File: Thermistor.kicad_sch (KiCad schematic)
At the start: 15 parts, among them U10 TLV6001DCK, U11 TLV6001DCK, U12 TLV6001DCK

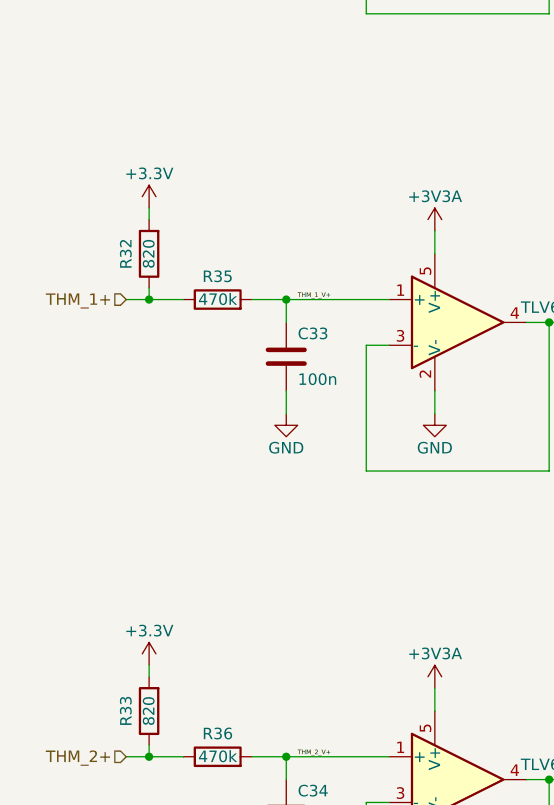
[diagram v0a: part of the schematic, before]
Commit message: Changed +3V3 to +3v3A for thermistor supplies
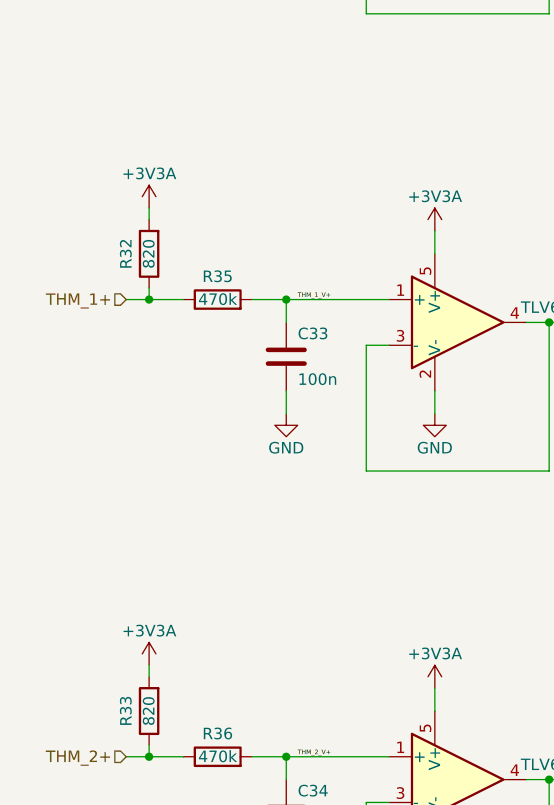
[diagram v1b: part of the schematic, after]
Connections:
- net +3.3V is gone; now on net +3V3A: R32.2, R33.2
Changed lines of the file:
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@@
-	)
-	(symbol
-		(lib_id "power:+3.3V")
-		(at 78.74 137.16 0)
-		(unit 1)
-		(exclude_from_sim no)
-		(in_bom yes)
-		(on_board yes)
-		(dnp no)
-		(property "Reference" "#PWR087"
-			(at 78.74 140.97 0)
-			(effects
-				(font
-					(size 1.27 1.27)
-				)
-				(hide yes)
-			)
-		)
-		(property "Value" "+3.3V"
-			(at 78.74 133.35 0)
-			(effects
-				(font
-					(size 1.27 1.27)
-				)
-			)
-		)
-		(property "Footprint" ""
-			(at 78.74 137.16 0)
-			(effects
-				(font
-					(size 1.27 1.27)
-				)
-				(hide yes)
-			)
-		)
-		(property "Datasheet" ""
-			(at 78.74 137.16 0)
-			(effects
-				(font
-					(size 1.27 1.27)
-				)
-				(hide yes)
-			)
-		)
-		(property "Description" "Power symbol creates a global label with name \"+3.3V\""
-			(at 78.74 137.16 0)
-			(effects
-				(font
-					(size 1.27 1.27)
-				)
-				(hide yes)
-			)
-		)
-		(pin "1"
-		)
-		(instances
-			(project "Motor_Control_Brain_Board"
-				(path "/7261d109-8405-40e9-921c-d95f374a7164/b4d68d60-4109-4352-9fbb-6372306ada14"
-					(reference "#PWR087")
-					(unit 1)
-				)
-			)
-		)
 	)
 	(symbol
@@
 	)
 	(symbol
+		(lib_id "power:+3.3VA")
+		(at 78.74 86.36 0)
+		(unit 1)
+		(exclude_from_sim no)
+		(in_bom yes)
+		(on_board yes)
+		(dnp no)
+		(property "Reference" "#PWR087"
+			(at 78.74 90.17 0)
+			(effects
+				(font
+					(size 1.27 1.27)
+				)
+				(hide yes)
+			)
+		)
+		(property "Value" "+3V3A"
+			(at 78.74 82.55 0)
+			(effects
+				(font
+					(size 1.27 1.27)
+				)
+			)
+		)
+		(property "Footprint" ""
+			(at 78.74 86.36 0)
+			(effects
+				(font
+					(size 1.27 1.27)
+				)
+				(hide yes)
+			)
+		)
+		(property "Datasheet" ""
+			(at 78.74 86.36 0)
+			(effects
+				(font
+					(size 1.27 1.27)
+				)
+				(hide yes)
+			)
+		)
+		(property "Description" "Power symbol creates a global label with name \"+3.3VA\""
+			(at 78.74 86.36 0)
+			(effects
+				(font
+					(size 1.27 1.27)
+				)
+				(hide yes)
+			)
+		)
+		(pin "1"
+		)
+		(instances
+			(project "motor-control-brain-board"
+				(path "/7261d109-8405-40e9-921c-d95f374a7164/b4d68d60-4109-4352-9fbb-6372306ada14"
+					(reference "#PWR087")
+					(unit 1)
+				)
+			)
+		)
+	)
+	(symbol
 		(lib_id "Device:R")
 		(at 82.55 45.72 90)
@@
 	)
 	(symbol
+		(lib_id "power:+3.3VA")
+		(at 78.74 137.16 0)
+		(unit 1)
+		(exclude_from_sim no)
+		(in_bom yes)
+		(on_board yes)
+		(dnp no)
+		(property "Reference" "#PWR086"
+			(at 78.74 140.97 0)
+			(effects
+				(font
+					(size 1.27 1.27)
+				)
+				(hide yes)
+			)
+		)
+		(property "Value" "+3V3A"
+			(at 78.74 133.35 0)
+			(effects
+				(font
+					(size 1.27 1.27)
+				)
+			)
+		)
+		(property "Footprint" ""
+			(at 78.74 137.16 0)
+			(effects
+				(font
+					(size 1.27 1.27)
+				)
+				(hide yes)
+			)
+		)
+		(property "Datasheet" ""
+			(at 78.74 137.16 0)
+			(effects
+				(font
+					(size 1.27 1.27)
+				)
+				(hide yes)
+			)
+		)
+		(property "Description" "Power symbol creates a global label with name \"+3.3VA\""
+			(at 78.74 137.16 0)
+			(effects
+				(font
+					(size 1.27 1.27)
+				)
+				(hide yes)
+			)
+		)
+		(pin "1"
+		)
+		(instances
+			(project "motor-control-brain-board"
+				(path "/7261d109-8405-40e9-921c-d95f374a7164/b4d68d60-4109-4352-9fbb-6372306ada14"
+					(reference "#PWR086")
+					(unit 1)
+				)
+			)
+		)
+	)
+	(symbol
 		(lib_id "power:GND")
 		(at 93.98 58.42 0)
@@
 					(unit 1)
 				)
-			)
-		)
-	)
-	(symbol
-		(lib_id "power:+3.3V")
-		(at 78.74 86.36 0)
-		(unit 1)
-		(exclude_from_sim no)
-		(in_bom yes)
-		(on_board yes)
-		(dnp no)
-		(property "Reference" "#PWR086"
-			(at 78.74 90.17 0)
-			(effects
-				(font
-					(size 1.27 1.27)
-				)
-				(hide yes)
-			)
-		)
-		(property "Value" "+3.3V"
-			(at 78.74 82.55 0)
-			(effects
-				(font
-					(size 1.27 1.27)
-				)
-			)
-		)
-		(property "Footprint" ""
-			(at 78.74 86.36 0)
-			(effects
-				(font
-					(size 1.27 1.27)
-				)
-				(hide yes)
-			)
-		)
-		(property "Datasheet" ""
-			(at 78.74 86.36 0)
-			(effects
-				(font
-					(size 1.27 1.27)
-				)
-				(hide yes)
-			)
-		)
-		(property "Description" "Power symbol creates a global label with name \"+3.3V\""
-			(at 78.74 86.36 0)
-			(effects
-				(font
-					(size 1.27 1.27)
-				)
-				(hide yes)
-			)
-		)
-		(pin "1"
-		)
-		(instances
-			(project "Motor_Control_Brain_Board"
-				(path "/7261d109-8405-40e9-921c-d95f374a7164/b4d68d60-4109-4352-9fbb-6372306ada14"
-					(reference "#PWR086")
-					(unit 1)
-				)
